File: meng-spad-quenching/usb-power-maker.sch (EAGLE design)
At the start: 3 parts, among them X1 PN61729-S

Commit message: Added pwr budget, boost controller IC
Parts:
- added C1, C100, C102, C3, C4, C96, C98: 0.1uF, Bogdan_Commons:C0603
- added C101, C99: 47uF, Bogdan_Commons:C0805
- added C103, C104, C106, C125, C126, C128: 10uF, Bogdan_Commons:C0805
- added C105, C107, C117, C118, C119, C121, C122, C123, C95: 0.01uF, Bogdan_Commons:C0603
- added C2: 1n, Bogdan_Commons:C0603
- added C5, C6, C7: VALUE, Bogdan_Commons:C0603
- added C97: 1uF, Bogdan_Commons:C0603
- added D1: CDBA140SL-HF, diode:DIODE-DO214AC
- added D4: BAT41ZFILM, diode:DIODE-SOD123
- added D5, D6: PMEG6010CEH,115, diode:DIODE-SOD123
- added IC1: LT1534, meng:LT1534
- added IC16: (no value), Kramnik's Library:LM5001
- added IC22: TPS7A3001, Kramnik's Library:TPS7A
- added IC24, IC25: TPS7A4901, Kramnik's Library:TPS7A
- added L5, L6: SRU2013-1R0Y, Kramnik's Library:SRU2013
- added R1, R2, R3, R4, R6, R7: VALUE, GadgetFactory:R0603
- added R5: 10R, GadgetFactory:R0603
- added R62: 10k, GadgetFactory:R0603
- added R63: 249R, GadgetFactory:R0603
- added R64: 16.5k, GadgetFactory:R0603
- added R65: 1.91k, GadgetFactory:R0603
- added R66: 20.5k, GadgetFactory:R0603
- added R74, R78: 87.6k, GadgetFactory:R0603
- added R75, R79: 11.8k, GadgetFactory:R0603
- added R76: 76.8k, GadgetFactory:R0603
- added R77: 24.0k, GadgetFactory:R0603
- added T1: RL-9400, Kramnik's Library:RL-9400
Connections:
- new net FLY_COMP_CH1: IC16.COMP, R63A.2
- new net FLY_FB_CH1: C96.2, IC16.FB, R64A.1, R65A.2
- new net FLY_FB_C_CH1: C96.1, R63A.1
- new net FLY_N12V0_CH1: C100.1, C101.1, D6.A, L6.P1, R64A.2
- new net FLY_NOUT_CH1: D6.C, T1.P4
- new net FLY_P12V0_CH1: C98.1, C99.1, D5.C, L5.P1
- new net FLY_POUT_CH1: D5.A, T1.P6
- new net FLY_RT_CH1: IC16.RT, R66A.2
- new net FLY_SNUBBER_CH1: C95.2, D4.C, R62A.1
- new net FLY_SW_CH1: D4.A, IC16.SW, T1.P3
- new net FLY_VCC_CH1: C97.1, IC16.VCC
- new net LDO_N10V0_FB_CH1: C123.2, IC22.FB, R78A.1, R79A.2
- new net LDO_N10V0_NR_SS_CH1: C118.1, IC22.NR/SS
- new net LDO_P10V0_FB_CH1: C121.2, IC24.FB, R74A.1, R75A.2
- new net LDO_P10V0_NR_SS_CH1: C117.1, IC24.NR/SS
- new net LDO_P5V0_FB_CH1: C122.2, IC25.FB, R76A.1, R77A.2
- new net LDO_P5V0_NR_SS_CH1: C119.1, IC25.NR/SS
- new net N$1: IC1.FB, R1A.2, R4A.2
- new net N$10: IC1.VIN
- new net N$11: D1.C, R4A.1
- new net N$12: IC1.NFB
- new net N$15: C6.1, IC1.VC, R7A.1
- new net N$16: IC1.RT, R6A.1
- new net N$17: C5.2, IC1.CT
- new net N$2: IC1.RCSL, R3A.2
- new net N$6: IC1.RVSL, R2A.2
- new net N$7: D1.A, IC1.COL, R5A.2
- new net N$8: C2.1, R5A.1
- new net N$9: C7.1, R7A.2
- new net PP_N10V0_ANALOG_CH1: C123.1, C126.1, C4.1, IC22.OUT, R78A.2
- new net PP_N12V0_ISO_CH1: C106.1, C107.1, IC22.EN, IC22.IN, L6.P2
- new net PP_P12V0_ISO_CH1: C104.1, C105.1, L5.P2
- new net PP_P15V0_ANALOG: C121.1, C125.1, C3.1, IC24.OUT, IC25.EN, IC25.IN, R74A.2
- new net PP_P16V0_BOOST: IC24.EN, IC24.IN
- new net PP_P5V0_ANALOG: C1.1, C122.1, C128.1, IC25.OUT, R76A.2
- new net PP_P5V0_LOGIC: C102.1, C103.1, C95.1, IC16.EN, IC16.VIN, R62A.2, T1.P1
- net GND: now also C1.2, C100.2, C101.2, C102.2, C103.2, C104.2, C105.2, C106.2, C107.2, C117.2, C118.2, C119.2, C125.2, C126.2, C128.2, C2.2, C3.2, C4.2, C5.1, C6.2, C7.2, C97.2, C98.2, C99.2, IC1.GND, IC1.PGND, IC16.GND, IC22.GND, IC24.GND, IC25.GND, R1A.1, R2A.1, R3A.1, R65A.1, R66A.1, R6A.2, R75A.1, R77A.1, R79A.1, T1.P5
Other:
- note added: "1 of 2"
- note added: "1.0"
- note added: "40mA MAX."
- note added: "ANALOG POWER SUPPLIES (CH. 1)"
- note added: "Channel 1 Analog Supply Postregulators"
- note added: "Channel 1 Analog Supply Split Flyback"
- note added: "Input Filter?"
- note added: "Layout Notes:"
- note added: "Note: 15V rail ratios need to be recalculated"
- note added: "Refer to TI/National RD-184 Reference Design for LM5001 Flyback Placement and Routing"
- note added: "TPS7A3001 (Negative)"
- note added: "TPS7A4901 (Positive)"
- note added: "Vout/(Rtop+Rbottom) > 5uA"
- note added: "Vref = -1.179V Nominal"
- note added: "Vref = 1.188V Nominal"
- note added: "Vref(1+Rtop/Rbottom) = Vout"

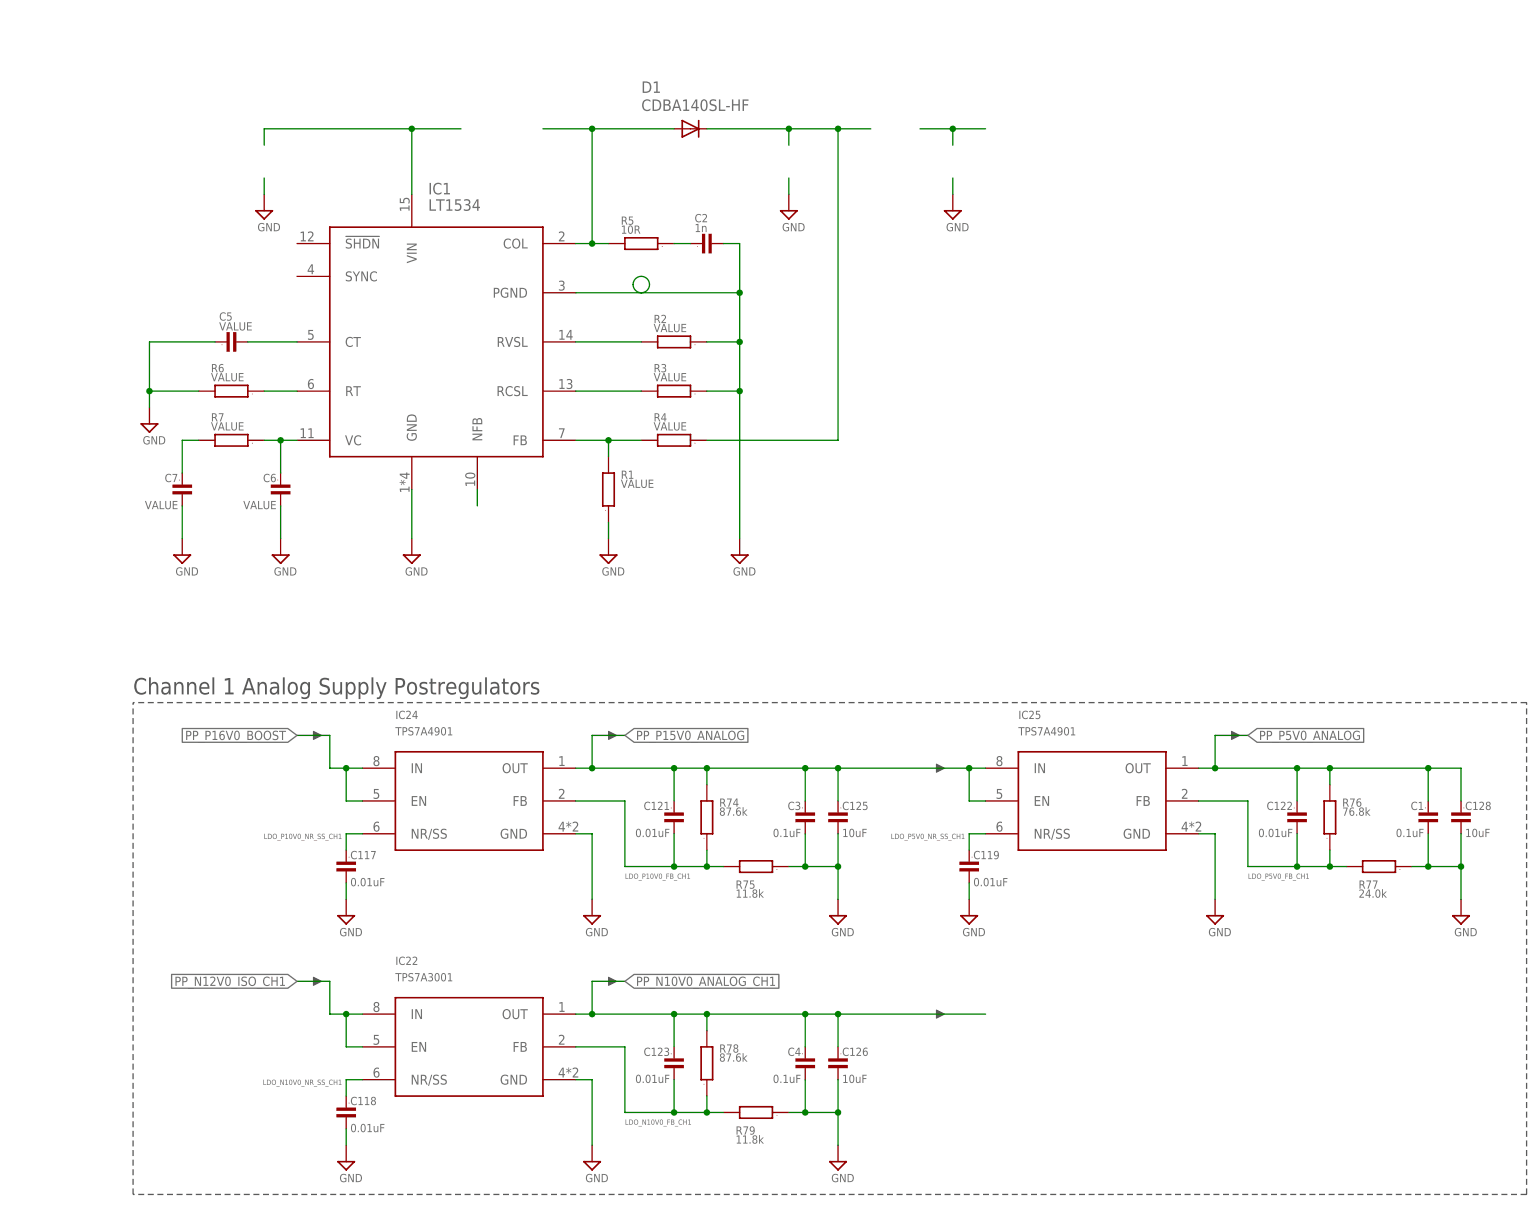
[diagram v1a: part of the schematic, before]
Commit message: Added SMT, Panel Mount SMA part numbers
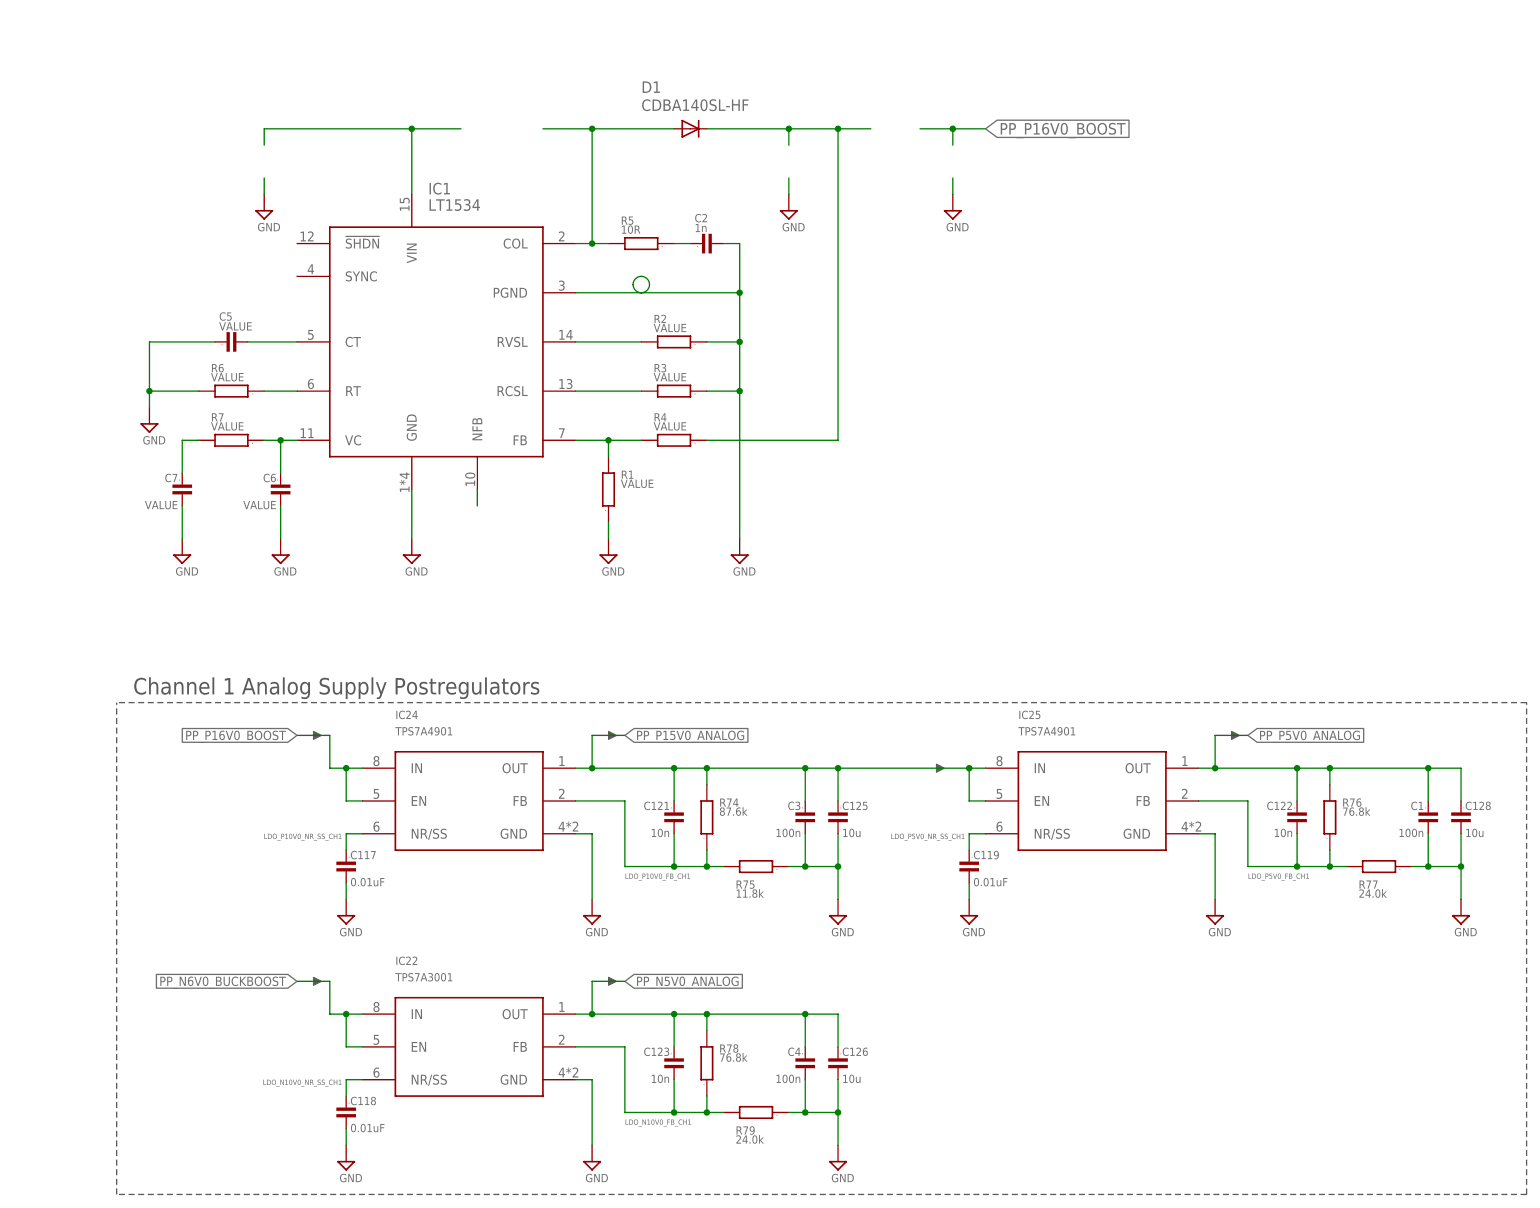
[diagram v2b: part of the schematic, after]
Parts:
- C1, C3, C4: value 0.1uF -> 100n
- C121, C122, C123: value 0.01uF -> 10n
- C125, C126, C128: value 10uF -> 10u
- R78: value 87.6k -> 76.8k
- R79: value 11.8k -> 24.0k
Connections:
- net PP_N10V0_ANALOG_CH1 renamed PP_N5V0_ANALOG
- new net PP_N6V0_BUCKBOOST: IC22.EN, IC22.IN
- net PP_N12V0_ISO_CH1: no longer IC22.EN, IC22.IN

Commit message: Added coupled inductor for Cuk converter
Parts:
- removed C100, C102, C96, C98: 0.1uF, Bogdan_Commons:C0603
- removed C101, C99: 47uF, Bogdan_Commons:C0805
- removed C103, C104, C106: 10uF, Bogdan_Commons:C0805
- removed C105, C107, C95: 0.01uF, Bogdan_Commons:C0603
- removed C97: 1uF, Bogdan_Commons:C0603
- removed D4: BAT41ZFILM, diode:DIODE-SOD123
- removed D5, D6: PMEG6010CEH,115, diode:DIODE-SOD123
- removed IC16: (no value), Kramnik's Library:LM5001
- removed L5, L6: SRU2013-1R0Y, Kramnik's Library:SRU2013
- removed R62: 10k, GadgetFactory:R0603
- removed R63: 249R, GadgetFactory:R0603
- removed R64: 16.5k, GadgetFactory:R0603
- removed R65: 1.91k, GadgetFactory:R0603
- removed R66: 20.5k, GadgetFactory:R0603
- removed T1: RL-9400, Kramnik's Library:RL-9400
- added C10, C8, C9: VALUE, Bogdan_Commons:C0603
- added C11: 1n, Bogdan_Commons:C0603
- added C12: 47u, Bogdan_Commons:C0805
- added C13, C14: 4.7u, Bogdan_Commons:C0805
- added C15, C16: 100n, Bogdan_Commons:C0603
- added D2: CDBA140SL-HF, diode:DIODE-DO214AC
- added IC2: LT1534-1, meng:LT1534
- added L3: SRF0703-220M, meng:SRF0703
- added R10, R11, R13, R14, R8, R9: VALUE, GadgetFactory:R0603
- added R12: 10R, GadgetFactory:R0603
- IC1: value LT1534 -> LT1534-1
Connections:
- removed net FLY_COMP_CH1: IC16.COMP, R63A.2
- removed net FLY_FB_CH1: C96.2, IC16.FB, R64A.1, R65A.2
- removed net FLY_FB_C_CH1: C96.1, R63A.1
- removed net FLY_N12V0_CH1: C100.1, C101.1, D6.A, L6.P1, R64A.2
- removed net FLY_NOUT_CH1: D6.C, T1.P4
- removed net FLY_P12V0_CH1: C98.1, C99.1, D5.C, L5.P1
- removed net FLY_POUT_CH1: D5.A, T1.P6
- removed net FLY_RT_CH1: IC16.RT, R66A.2
- removed net FLY_SNUBBER_CH1: C95.2, D4.C, R62A.1
- removed net FLY_SW_CH1: D4.A, IC16.SW, T1.P3
- removed net FLY_VCC_CH1: C97.1, IC16.VCC
- removed net PP_N12V0_ISO_CH1: C106.1, C107.1, L6.P2
- removed net PP_N6V0_BUCKBOOST: IC22.EN, IC22.IN
- removed net PP_P12V0_ISO_CH1: C104.1, C105.1, L5.P2
- removed net PP_P5V0_LOGIC: C102.1, C103.1, C95.1, IC16.EN, IC16.VIN, R62A.2, T1.P1
- new net N$13: IC1.FB
- new net N$14: IC1.RCSL, R10A.2
- new net N$18: IC1.RVSL, R9A.2
- new net N$19: C12.2, D2.A, L3.4
- new net N$20: C11.1, R12A.1
- new net N$21: C14.1, IC1.VIN, L3.1
- new net N$23: C10.1, R14A.2
- new net N$24: C9.1, IC1.VC, R14A.1
- new net N$25: IC1.RT, R13A.1
- new net N$26: C8.2, IC1.CT
- new net N$27: IC1.NFB, R11A.2, R8A.2
- new net N$28: C12.1, IC1.COL, L3.3, R12A.2
- new net PP_N6V0_CUK: C13.1, C16.1, IC22.EN, IC22.IN, L3.2, R11A.1
- net GND: now also C10.2, C11.2, C13.2, C14.2, C15.2, C16.2, C8.1, C9.2, D2.C, IC2.GND, IC2.PGND, R10A.1, R13A.2, R8A.1, R9A.1; no longer C100.2, C101.2, C102.2, C103.2, C104.2, C105.2, C106.2, C107.2, C97.2, C98.2, C99.2, IC16.GND, R65A.1, R66A.1, T1.P5
- net N$1: now also IC2.FB; no longer IC1.FB
- net N$10: now also IC2.VIN; no longer IC1.VIN
- net N$12: now also IC2.NFB; no longer IC1.NFB
- net N$15: now also IC2.VC; no longer IC1.VC
- net N$16: now also IC2.RT; no longer IC1.RT
- net N$17: now also IC2.CT; no longer IC1.CT
- net N$2: now also IC2.RCSL; no longer IC1.RCSL
- net N$6: now also IC2.RVSL; no longer IC1.RVSL
- net N$7: now also IC2.COL; no longer IC1.COL
- net PP_P16V0_BOOST: now also C15.1
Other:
- note added: "25nH"
- note added: "Analog Supply Postregulators"
- note removed: "40mA MAX."
- note removed: "Channel 1 Analog Supply Postregulators"
- note removed: "Channel 1 Analog Supply Split Flyback"
- note removed: "Input Filter?"
- moved on the sheet: C1, C117, C118, C119, C121, C122, C123, C125, C126, C128, C2, C3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

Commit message: Work on SEPIC converter
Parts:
- added C17: DNP, Bogdan_Commons:C0603
- C10: value VALUE -> 33n
- C11: value 1n -> 10n
- C8: value VALUE -> 1300p
- C9: value VALUE -> DNP
- L3: value SRF0703-220M -> SRF0703-820M
- R10, R8, R9: value VALUE -> 1k
- R11: value VALUE -> 1.41k
- R12: value 10R -> 100R
- R13: value VALUE -> 16.9k
- R14: value VALUE -> 2k
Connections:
- net N$3 renamed USBCONN_P1
- net N$4 renamed USBCONN_P4
- removed net N$10: IC2.VIN
- removed net N$21: C14.1, IC1.VIN, L3.1
- removed net N$5: L1.P$2
- new net !SHDN_BOOST: IC2.!SHDN
- new net !SHDN_CUK: IC1.!SHDN
- new net USB_VDD: C14.1, IC1.VIN, IC2.VIN, L1.P$2, L3.1
- net GND: now also C17.2
- net N$19: now also C17.1
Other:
- note added: "-2.5V Nom."
- note added: "1 of 1"
- note added: "USB POWER MAKER"
- note removed: "1 of 2"
- note removed: "ANALOG POWER SUPPLIES (CH. 1)"
- moved on the sheet: C13, C2, C5, C6, C7, D1, IC2, R1, R11, R2, R3, R4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
